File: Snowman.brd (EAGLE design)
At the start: 38.1 x 58.4 mm, 11 parts, among them J1 ICSP, U1 ATtiny85

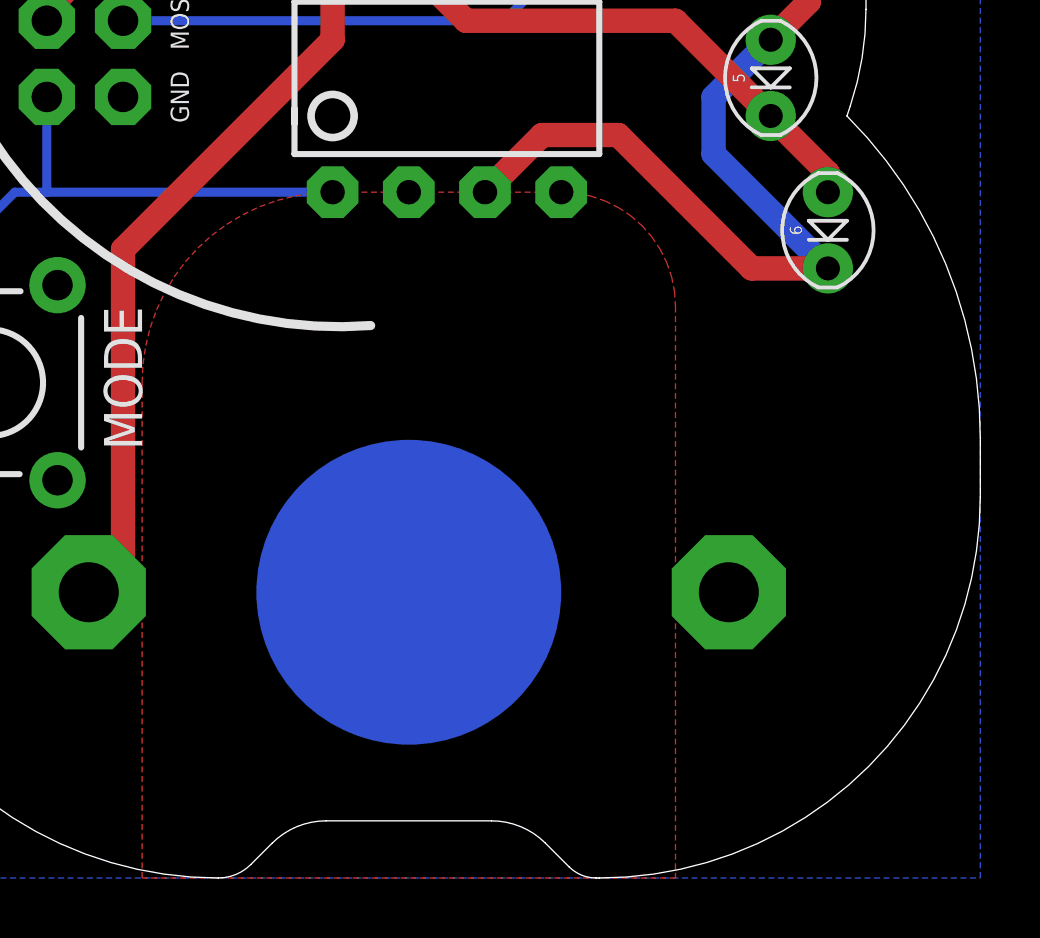
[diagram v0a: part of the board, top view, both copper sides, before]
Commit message: updating adding pullup
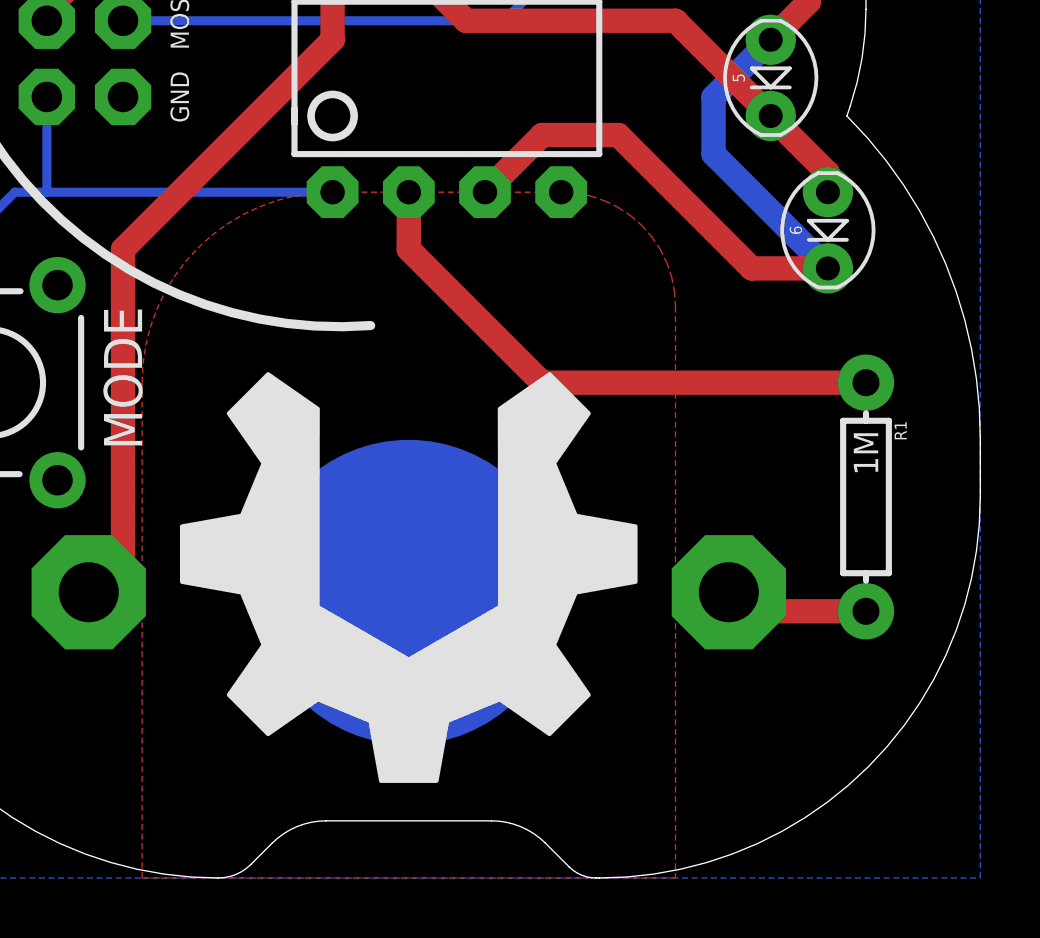
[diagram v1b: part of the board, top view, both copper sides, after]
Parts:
- added R1: 1M, barbary_enterprises:AXIAL-0.3
- added U$2: USER_HACKABLE, logo:USER_HACKABLE
- U$1: value CR2032 -> (none)
- renumbered BATT to U$1
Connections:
- new net VCC`: R1.P$2, U$1.+2
- net D3: now also R1.P$1
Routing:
- net D3: track 0.00 -> 19.0 mm
- net VCC`: track 0.00 -> 4.84 mm
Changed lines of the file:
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@@
 <layer number="56" name="wert" color="7" fill="1" visible="no" active="no"/>
 <layer number="57" name="tCAD" color="7" fill="1" visible="no" active="no"/>
+<layer number="59" name="tCarbon" color="7" fill="1" visible="no" active="no"/>
+<layer number="60" name="bCarbon" color="7" fill="1" visible="no" active="no"/>
 <layer number="90" name="Modules" color="5" fill="1" visible="no" active="no"/>
 <layer number="91" name="Nets" color="2" fill="1" visible="no" active="no"/>
@@
 <layer number="113" name="IDFDebug" color="7" fill="1" visible="yes" active="yes"/>
 <layer number="116" name="Patch_BOT" color="9" fill="4" visible="yes" active="yes"/>
+<layer number="118" name="Rect_Pads" color="7" fill="1" visible="no" active="no"/>
 <layer number="121" name="_tsilk" color="7" fill="1" visible="yes" active="yes"/>
 <layer number="122" name="_bsilk" color="7" fill="1" visible="yes" active="yes"/>
@@
 <layer number="127" name="_tValues" color="7" fill="1" visible="yes" active="yes"/>
 <layer number="128" name="_bValues" color="7" fill="1" visible="yes" active="yes"/>
+<layer number="129" name="Mask" color="7" fill="1" visible="yes" active="yes"/>
 <layer number="131" name="tAdjust" color="7" fill="1" visible="yes" active="yes"/>
 <layer number="132" name="bAdjust" color="7" fill="1" visible="yes" active="yes"/>
@@
 <layer number="230" name="230bmp" color="7" fill="1" visible="yes" active="yes"/>
 <layer number="231" name="231bmp" color="7" fill="1" visible="yes" active="yes"/>
+<layer number="232" name="Eagle3D_PG2" color="7" fill="1" visible="no" active="no"/>
+<layer number="233" name="Eagle3D_PG3" color="7" fill="1" visible="no" active="no"/>
 <layer number="248" name="Housing" color="7" fill="1" visible="yes" active="yes"/>
 <layer number="249" name="Edge" color="7" fill="1" visible="yes" active="yes"/>
@@
 <element name="4" library="barbary_enterprises" package="LED-OVAL" value="" x="30.48" y="31.75" rot="R90"/>
 <element name="5" library="barbary_enterprises" package="LED-OVAL" value="" x="31.115" y="26.67" rot="R90"/>
-<element name="BATT" library="battery" package="CR2032-THRU" value="CR2032" x="19.05" y="9.525" smashed="yes" rot="MR180">
-<attribute name="VALUE" x="14.097" y="21.59" size="1.6764" layer="28" font="vector" rot="MR180"/>
-</element>
 <element name="J1" library="barbary_enterprises" package="2X3-NS" value="ICSP" x="8.255" y="28.575" rot="R270"/>
 <element name="MODE" library="barbary_enterprises" package="TACTILE-PTH" value="" x="5.08" y="16.51" rot="R270"/>
@@
 <attribute name="VALUE" x="20.955" y="20.955" size="1.27" layer="27" ratio="10" align="center"/>
 </element>
+<element name="R1" library="barbary_enterprises" package="AXIAL-0.3" value="1M" x="34.29" y="12.7" rot="R270"/>
+<element name="U$1" library="battery" package="CR2032-THRU" value="" x="19.05" y="9.525" smashed="yes" rot="MR180">
+<attribute name="VALUE" x="14.732" y="15.875" size="1.6764" layer="28" font="vector" rot="MR180"/>
+</element>
+<element name="U$2" library="logo" package="USER_HACKABLE" value="USER_HACKABLE" x="19.05" y="10.795"/>
 </elements>
 <signals>
 <signal name="GND">
-<contactref element="BATT" pad="-"/>
 <contactref element="U1" pad="4"/>
 <contactref element="MODE" pad="1"/>
@@
 </polygon>
 <contactref element="MODE" pad="2"/>
+<contactref element="U$1" pad="-"/>
 </signal>
 <signal name="RST">
@@
 <signal name="VCC">
 <contactref element="U1" pad="8"/>
-<contactref element="BATT" pad="+1"/>
 <contactref element="J1" pad="2"/>
 <wire x1="8.382" y1="9.525" x2="8.382" y2="9.652" width="0.8128" layer="1"/>
@@
 <wire x1="16.51" y1="30.48" x2="15.875" y2="31.115" width="0.8128" layer="1"/>
 <wire x1="15.875" y1="31.115" x2="9.525" y2="31.115" width="0.8128" layer="1"/>
+<contactref element="U$1" pad="+1"/>
 </signal>
 <signal name="D0">
@@
 <vertex x="27.94" y="0"/>
 </polygon>
+<contactref element="R1" pad="P$1"/>
+<wire x1="34.29" y1="16.51" x2="23.495" y2="16.51" width="0.8128" layer="1"/>
+<wire x1="23.495" y1="16.51" x2="19.05" y2="20.955" width="0.8128" layer="1"/>
+<wire x1="19.05" y1="20.955" x2="19.05" y2="22.86" width="0.8128" layer="1"/>
 </signal>
 <signal name="D4">
@@
 <wire x1="28.575" y1="33.02" x2="27.305" y2="34.29" width="0.8128" layer="1"/>
 </signal>
+<signal name="VCC`">
+<contactref element="R1" pad="P$2"/>
+<contactref element="U$1" pad="+2"/>
+<wire x1="34.29" y1="8.89" x2="30.353" y2="8.89" width="0.8128" layer="1"/>
+<wire x1="30.353" y1="8.89" x2="29.718" y2="9.525" width="0.8128" layer="1"/>
+</signal>
 </signals>

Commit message: 4H logo
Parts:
- U$2: value USER_HACKABLE -> 18 USC 707; device logo:USER_HACKABLE -> 4h:4H_LOGO_6
- moved U$2 0.63 mm to (19.1, 10.2)
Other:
- board text added: "Cache Makers cachemakers.org"
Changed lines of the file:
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@@
 <vertex x="9.8425" y="46.6725"/>
 </polygon>
+<text x="12.7" y="34.29" size="1.016" layer="21" align="center">Cache Makers
+cachemakers.org</text>
 </plain>
 <attributes>
@@
 <attribute name="VALUE" x="14.732" y="15.875" size="1.6764" layer="28" font="vector" rot="MR180"/>
 </element>
-<element name="U$2" library="logo" package="USER_HACKABLE" value="USER_HACKABLE" x="19.05" y="10.795"/>
+<element name="U$2" library="4h" package="4H_LOGO_6" value="18 USC 707" x="19.05" y="10.16"/>
 </elements>
 <signals>
